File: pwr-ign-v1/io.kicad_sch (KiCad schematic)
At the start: 135 parts, among them J1 DIG-in, P1 IN-CPU, P10 LSD-CPU, P11 INJECTORS, P12 LSDS, P2 OUT_GND, P3 TRIG-cpu, P4 DIG-CPU, P5 CPU_PWR, P6 IGNITION, P7 TRIG-IN, P8 PWR_IN, P9 INJ-CPU, Q1 MOSFET, Q2 MOSFET, Q3 MOSFET, Q4 MOSFET, Q5 MOSFET, Q6 MOSFET, Q7 MOSFET, Q8 MOSFET, U1 LM2940, U2 MIC4469, U3 MAX9926UAEE+, U4 MIC4469, U5 MIC4469

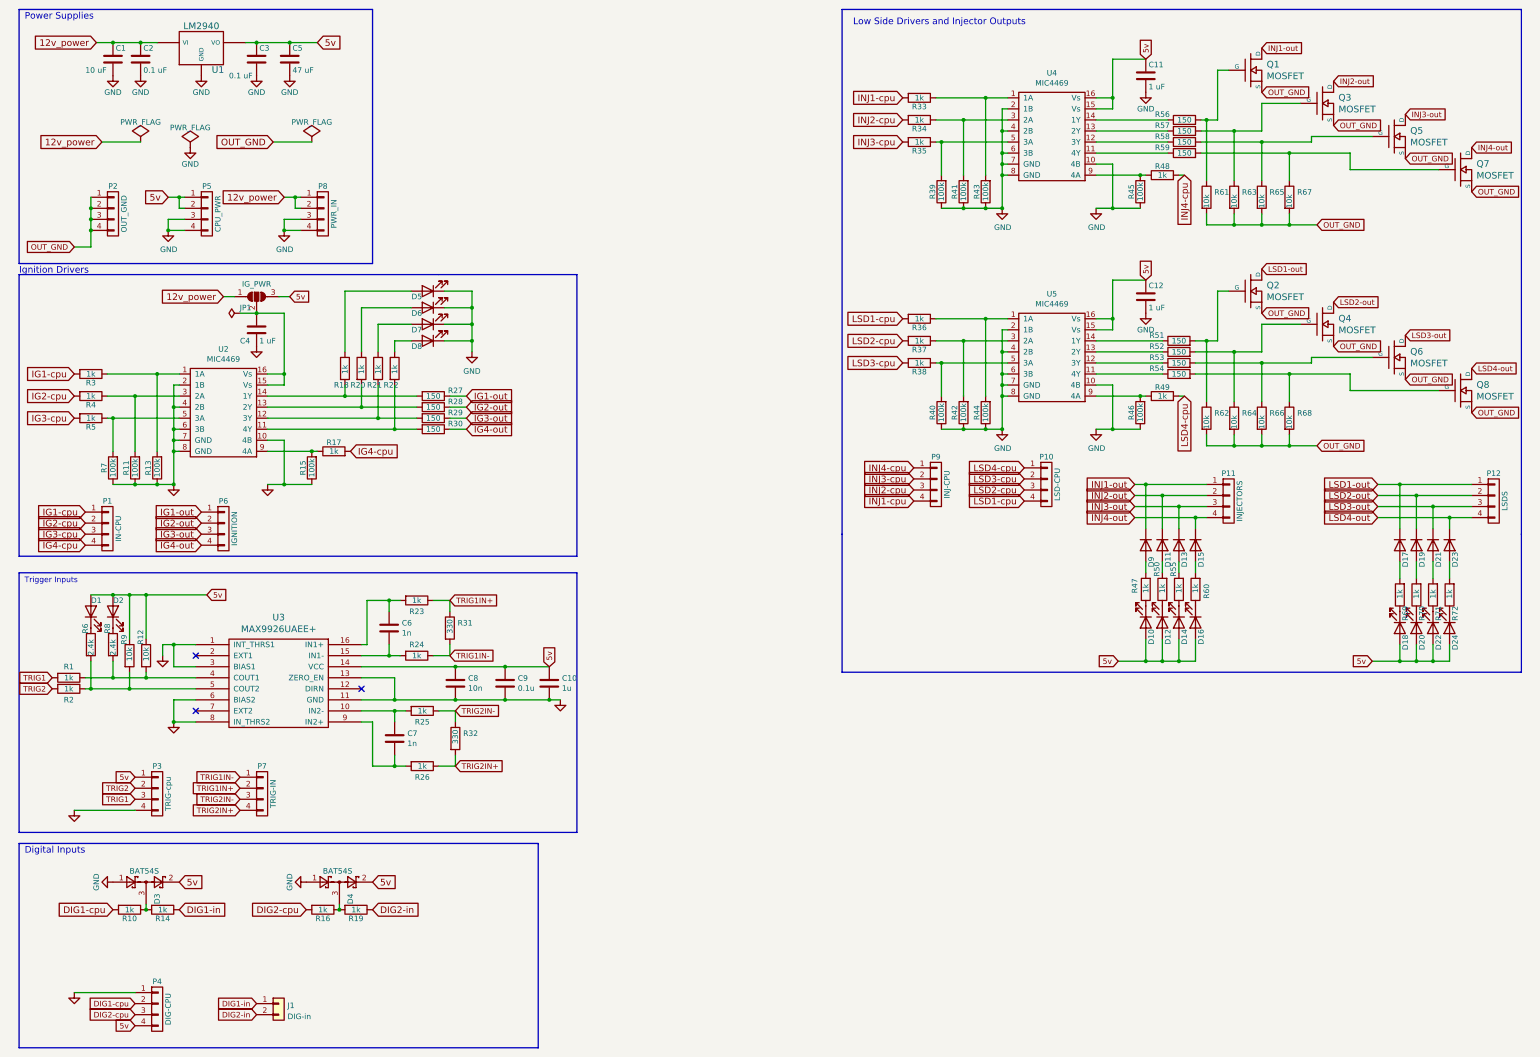
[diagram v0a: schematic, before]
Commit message: Add "Ignition V1" board for power supply, 4x ignition outputs, 2x VR inputs, and 2 digital inputs
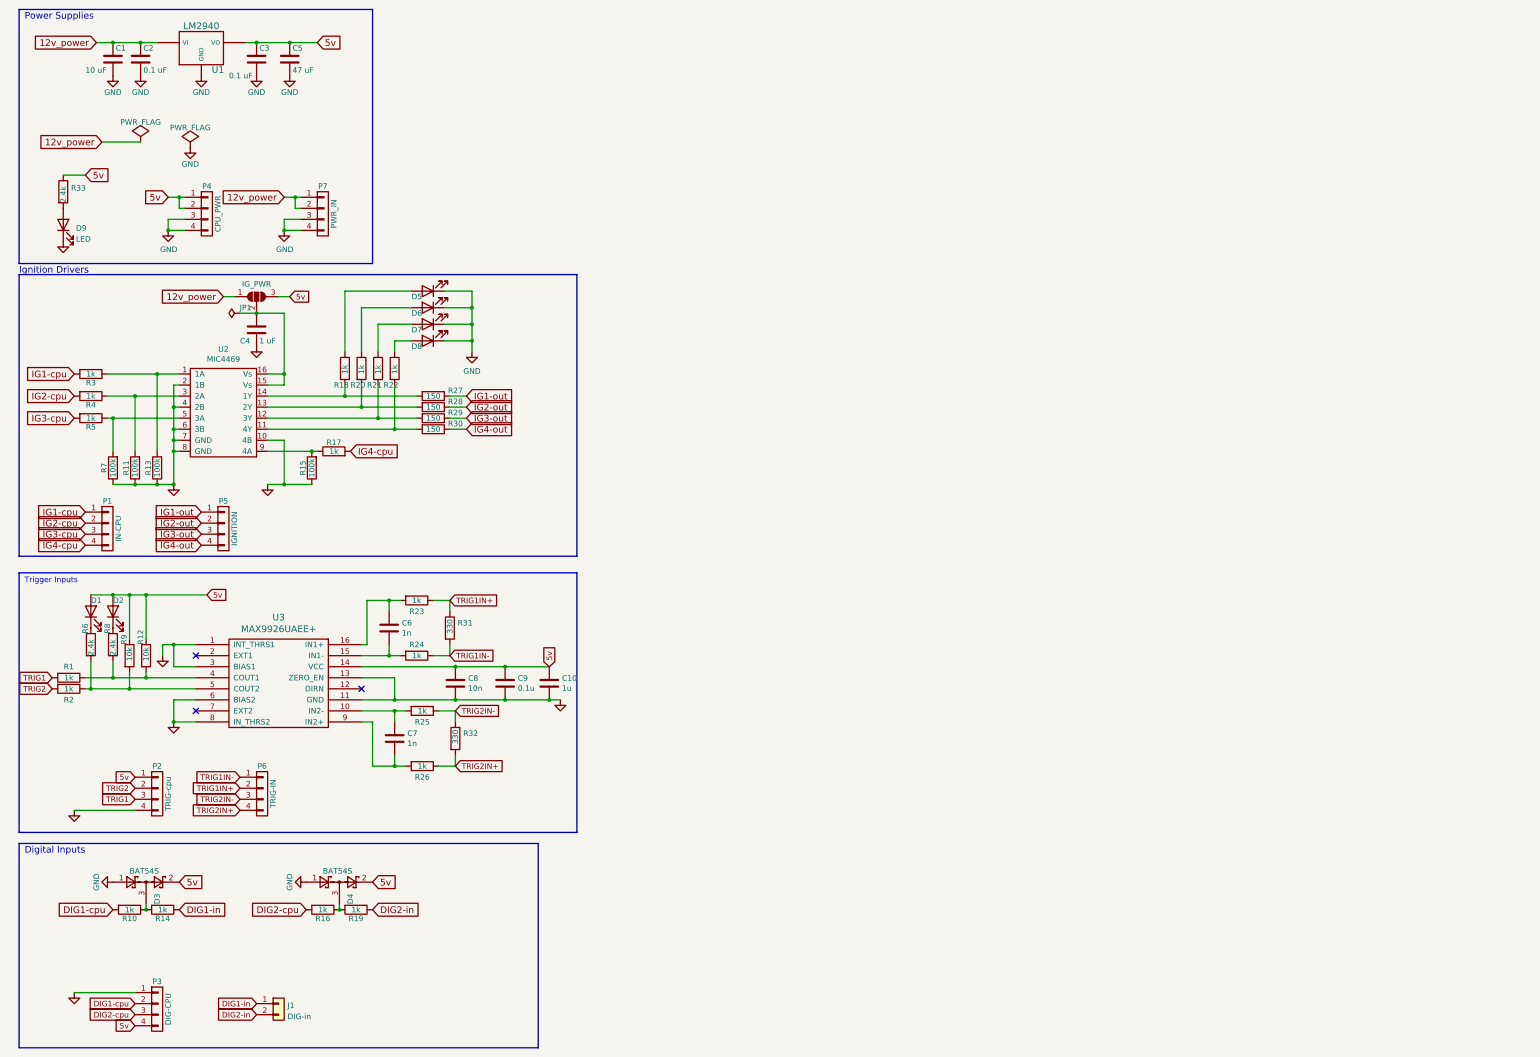
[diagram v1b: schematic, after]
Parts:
- removed C11, C12: 1 uF, Capacitor_SMD:C_0805_2012Metric_Pad1.18x1.45mm_HandSolder, symbol io-rescue:C-io-rescue-io-rescue
- removed D10, D12, D14, D16, D18, D20, D22, D24: LED, LED_SMD:LED_0805_2012Metric_Pad1.15x1.40mm_HandSolder, symbol Device:LED
- removed D11, D13, D15, D17, D19, D21, D23, D9: 1N4148, Diode_SMD:D_0805_2012Metric_Pad1.15x1.40mm_HandSolder, symbol Diode:1N4148
- removed P10: LSD-CPU, Connector_PinHeader_2.54mm:PinHeader_1x04_P2.54mm_Vertical, symbol io-rescue:CONN_01X04-io-rescue-io-rescue
- removed P11: INJECTORS, Connector_PinHeader_2.54mm:PinHeader_1x04_P2.54mm_Vertical, symbol io-rescue:CONN_01X04-io-rescue-io-rescue
- removed P12: LSDS, Connector_PinHeader_2.54mm:PinHeader_1x04_P2.54mm_Vertical, symbol io-rescue:CONN_01X04-io-rescue-io-rescue
- removed P2: OUT_GND, Connector_PinHeader_2.54mm:PinHeader_1x04_P2.54mm_Vertical, symbol io-rescue:CONN_01X04-io-rescue-io-rescue
- removed P9: INJ-CPU, Connector_PinHeader_2.54mm:PinHeader_1x04_P2.54mm_Vertical, symbol io-rescue:CONN_01X04-io-rescue-io-rescue
- removed Q1, Q2, Q3, Q4, Q5, Q6, Q7, Q8: MOSFET, Package_TO_SOT_SMD:TO-252-2, symbol io-rescue:VND14NV04-io-rescue-io-rescue
- removed R33, R34, R35, R36, R37, R38, R48, R49: 1k, Resistor_SMD:R_0805_2012Metric_Pad1.20x1.40mm_HandSolder, symbol io-rescue:R-io-rescue-io-rescue
- removed R39, R40, R41, R42, R43, R44, R45, R46: 100k, Resistor_SMD:R_0805_2012Metric_Pad1.20x1.40mm_HandSolder, symbol io-rescue:R-io-rescue-io-rescue
- removed R47, R50, R55, R60, R69, R70, R71, R72: 1k, Resistor_SMD:R_0805_2012Metric_Pad1.20x1.40mm_HandSolder, symbol Device:R
- removed R51, R52, R53, R54, R56, R57, R58, R59: 150, Resistor_SMD:R_0805_2012Metric_Pad1.20x1.40mm_HandSolder, symbol Device:R
- removed R61, R62, R63, R64, R65, R66, R67, R68: 10k, Resistor_SMD:R_0805_2012Metric_Pad1.20x1.40mm_HandSolder, symbol io-rescue:R-analog-rescue
- removed U4, U5: MIC4469, Package_SO:SOIC-16W_7.5x10.3mm_P1.27mm, symbol io-rescue:MIC4469-viaems-io-rescue
- added D9: LED, LED_SMD:LED_0805_2012Metric_Pad1.15x1.40mm_HandSolder, symbol Device:LED
- added R33: 2.4k, Resistor_SMD:R_0805_2012Metric_Pad1.20x1.40mm_HandSolder, symbol Device:R
- renumbered P3 to P2, P4 to P3, P5 to P4, P6 to P5, P7 to P6, P8 to P7
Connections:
- net 5v: now also R33.1
- net GND: now also D9.1 (K)
- new net: D9.2 (A), R33.2
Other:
- note removed: "Low Side Drivers and Injector Outputs"
